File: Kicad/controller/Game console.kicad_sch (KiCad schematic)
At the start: 6 parts, among them SW1 SW_Push, SW2 SW_Push, SW3 SW_Push

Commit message: writing firmware codee
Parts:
- removed RV1, RV2: R_Potentiometer, symbol Device:R_Potentiometer
- removed SW1, SW2: SW_Push, symbol Switch:SW_Push
- added C1, C2: 100nF, Capacitor_THT:C_Disc_D5.0mm_W2.5mm_P2.50mm, symbol Device:C
- added Left1, Right1: RKJXV1224005, easyeda2kicad:SW-TH_RKJXV1224005, symbol easyeda2kicad:RKJXV1224005
- added SW1: LB, easyeda2kicad:SW-TH_TC-1102N-C-DL-B, symbol easyeda2kicad:TC-1102N-C-DL-B
- added SW10: B, Button_Switch_THT:SW_PUSH_6mm_H5mm, symbol Switch:SW_Push
- added SW11: Menu, Button_Switch_THT:SW_PUSH_6mm_H5mm, symbol Switch:SW_Push
- added SW12: X, Button_Switch_THT:SW_PUSH_6mm_H5mm, symbol Switch:SW_Push
- added SW13: Y, Button_Switch_THT:SW_PUSH_6mm_H5mm, symbol Switch:SW_Push
- added SW14: View, Button_Switch_THT:SW_PUSH_6mm_H5mm, symbol Switch:SW_Push
- added SW15: LT, easyeda2kicad:SW-TH_TC-1102N-C-DL-B, symbol easyeda2kicad:TC-1102N-C-DL-B
- added SW16: RT, easyeda2kicad:SW-TH_TC-1102N-C-DL-B, symbol easyeda2kicad:TC-1102N-C-DL-B
- added SW2: RB, easyeda2kicad:SW-TH_TC-1102N-C-DL-B, symbol easyeda2kicad:TC-1102N-C-DL-B
- added SW4: D Pad right, Button_Switch_THT:SW_PUSH_6mm_H5mm, symbol Switch:SW_Push
- added SW5: D Pad Left, Button_Switch_THT:SW_PUSH_6mm_H5mm, symbol Switch:SW_Push
- added SW6: A, Button_Switch_THT:SW_PUSH_6mm_H5mm, symbol Switch:SW_Push
- added SW7: D Pad bottom, Button_Switch_THT:SW_PUSH_6mm_H5mm, symbol Switch:SW_Push
- added SW8: Reset, Button_Switch_THT:SW_PUSH_6mm_H5mm, symbol Switch:SW_Push
- added SW9: Home, Button_Switch_THT:SW_PUSH_6mm_H5mm, symbol Switch:SW_Push
- added U1: MCP3008, Package_DIP:DIP-16_W7.62mm, symbol Analog_ADC:MCP3008
- SW3: value SW_Push -> D Pad top; footprint (none) -> Button_Switch_THT:SW_PUSH_6mm_H5mm
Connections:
- net at SW3.1: now also A1.19 (GPIO14)
- net at SW3.2: now also A1.13 (GND), A1.18 (GND), A1.23 (GND), A1.28 (GND), A1.3 (GND), A1.33 (AGND), A1.38 (GND), A1.8 (GND), C1.2, C2.2, Left1.1 (B), Left1.10 (GND), Left1.6 (B), Left1.7 (GND), Left1.8 (GND), Left1.9 (GND), Left1.b, Right1.1 (B), Right1.10 (GND), Right1.6 (B), Right1.7 (GND), Right1.8 (GND), Right1.9 (GND), Right1.b, SW1.2, SW1.3, SW1.4, SW10.2, SW11.2, SW12.2, SW13.2, SW14.2, SW15.2, SW15.3, SW15.4, SW16.2, SW16.3, SW16.4, SW2.2, SW2.3, SW2.4, SW4.2, SW5.2, SW6.2, SW7.2, SW8.2, SW9.2, U1.14 (AGND), U1.9 (DGND)
- net at A1.36 (3V3): now also C1.1, C2.1, Left1.3 (A), Left1.4 (A), Right1.3 (A), Right1.4 (A), U1.15 (Vref), U1.16 (Vdd)
- net at A1.1 (GPIO0): now also SW14.1
- net at A1.10 (GPIO7): now also SW13.1
- net at A1.11 (GPIO8): now also SW12.1
- net at A1.12 (GPIO9): now also SW10.1
- net at A1.14 (GPIO10): now also SW6.1
- net at A1.15 (GPIO11): now also SW4.1
- net at A1.16 (GPIO12): now also SW5.1
- net at A1.17 (GPIO13): now also SW7.1
- net at A1.2 (GPIO1): now also SW9.1
- net at A1.21 (GPIO16): now also U1.12 (Dout)
- net at A1.22 (GPIO17): now also U1.10 (~{CS}/SHDN)
- net at A1.24 (GPIO18): now also U1.13 (CLK)
- net at A1.25 (GPIO19): now also U1.11 (Din)
- net at A1.30 (RUN): now also SW8.1
- net at A1.31 (GPIO26_ADC0): now also Left1.a
- net at A1.32 (GPIO27_ADC1): now also Right1.a
- net at A1.4 (GPIO2): now also SW11.1
- net at A1.5 (GPIO3): now also SW16.1
- net at A1.6 (GPIO4): now also SW2.1
- net at A1.7 (GPIO5): now also SW15.1
- net at A1.9 (GPIO6): now also SW1.1
- new net: Left1.2 (DTA), U1.1 (CH0)
- new net: Left1.5 (DTA), U1.2 (CH1)
- new net: Right1.2 (DTA), U1.3 (CH2)
- new net: Right1.5 (DTA), U1.4 (CH3)
- no-connect marks 0 -> 17

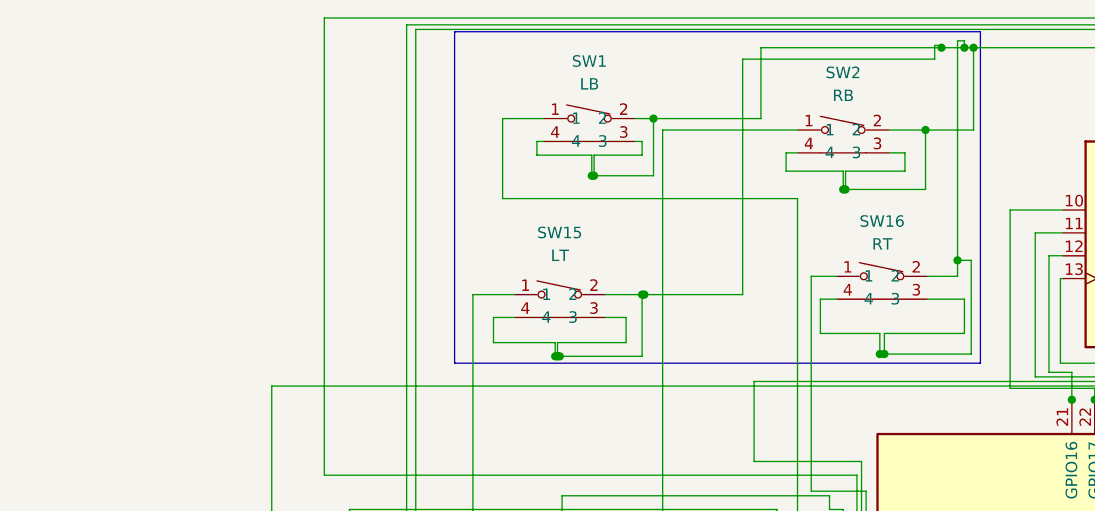
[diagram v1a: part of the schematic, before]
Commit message: basic cad complete and new shoulder board created for rb, lb, rt and lt triggers
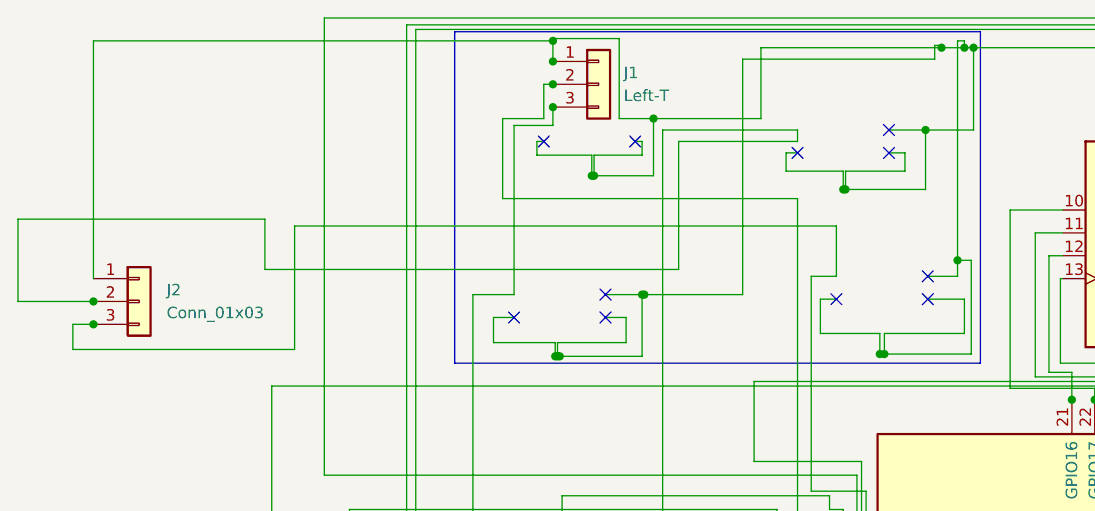
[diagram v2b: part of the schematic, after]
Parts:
- removed SW1: LB, easyeda2kicad:SW-TH_TC-1102N-C-DL-B, symbol easyeda2kicad:TC-1102N-C-DL-B
- removed SW15: LT, easyeda2kicad:SW-TH_TC-1102N-C-DL-B, symbol easyeda2kicad:TC-1102N-C-DL-B
- removed SW16: RT, easyeda2kicad:SW-TH_TC-1102N-C-DL-B, symbol easyeda2kicad:TC-1102N-C-DL-B
- removed SW2: RB, easyeda2kicad:SW-TH_TC-1102N-C-DL-B, symbol easyeda2kicad:TC-1102N-C-DL-B
- added J1: Left-T, Connector_JST:JST_XH_B3B-XH-A_1x03_P2.50mm_Vertical, symbol Connector_Generic:Conn_01x03
- added J2: Conn_01x03, Connector_JST:JST_XH_B3B-XH-A_1x03_P2.50mm_Vertical, symbol Connector_Generic:Conn_01x03
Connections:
- net at A1.13 (GND), A1.18 (GND), A1.23 (GND)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: now also J1.1 (Pin_1), J2.1 (Pin_1)
- net at A1.6 (GPIO4): now also J2.2 (Pin_2)
- net at A1.9 (GPIO6): now also J1.2 (Pin_2)
- net at A1.5 (GPIO3): now also J2.3 (Pin_3)
- net at A1.7 (GPIO5): now also J1.3 (Pin_3)
- no-connect marks 17 -> 28

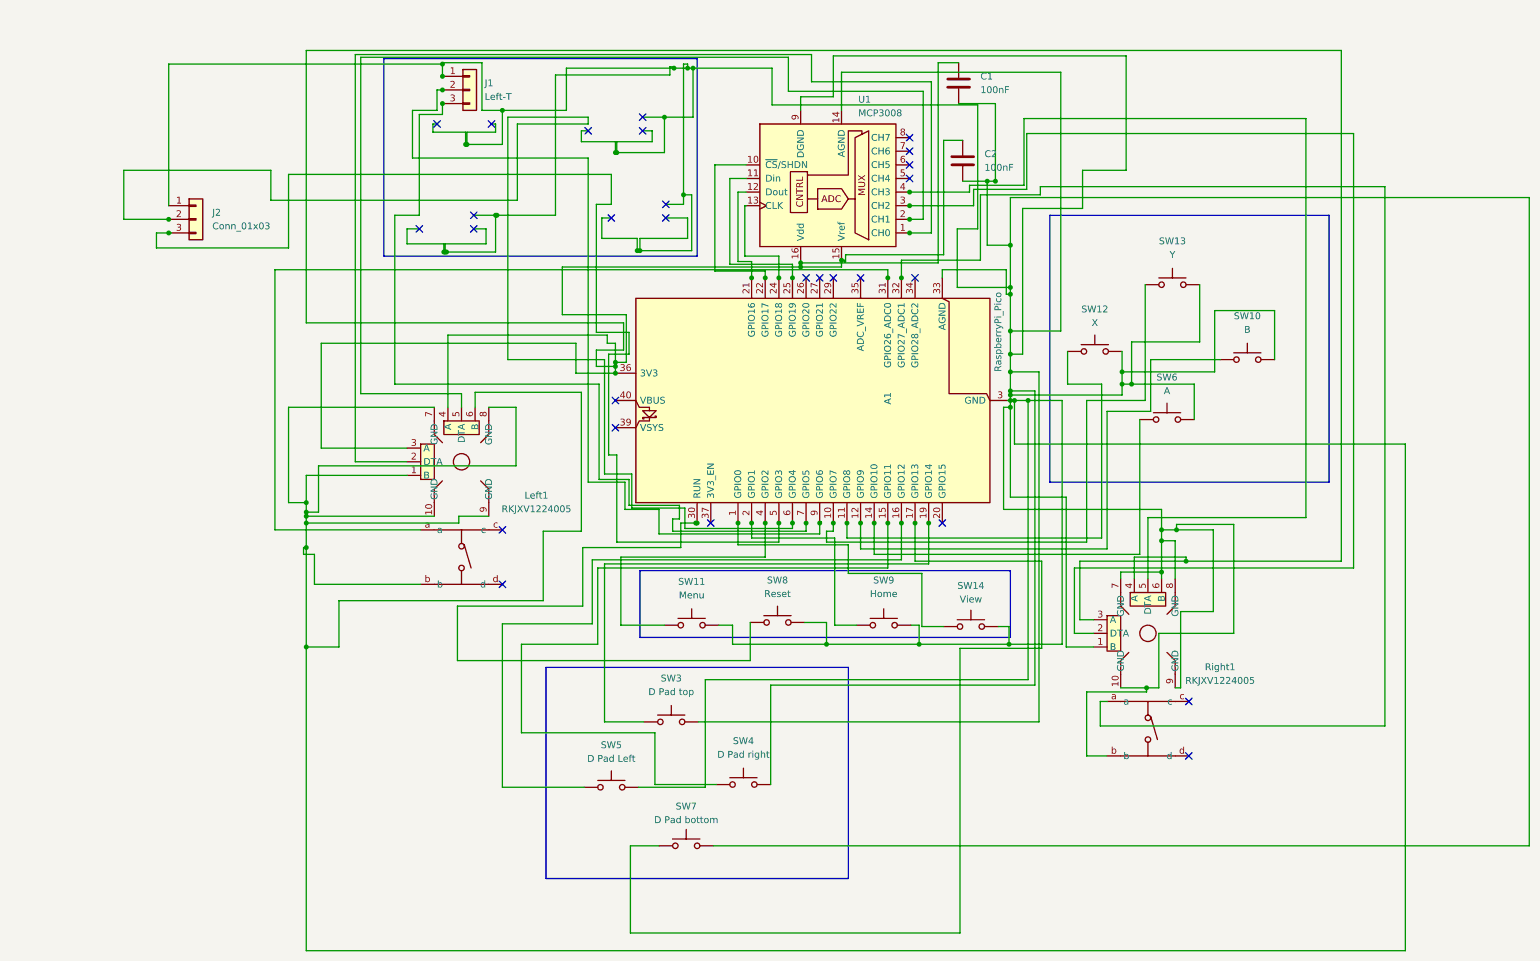
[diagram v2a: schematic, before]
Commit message: changes in schematic to add vibration motors for controller and led
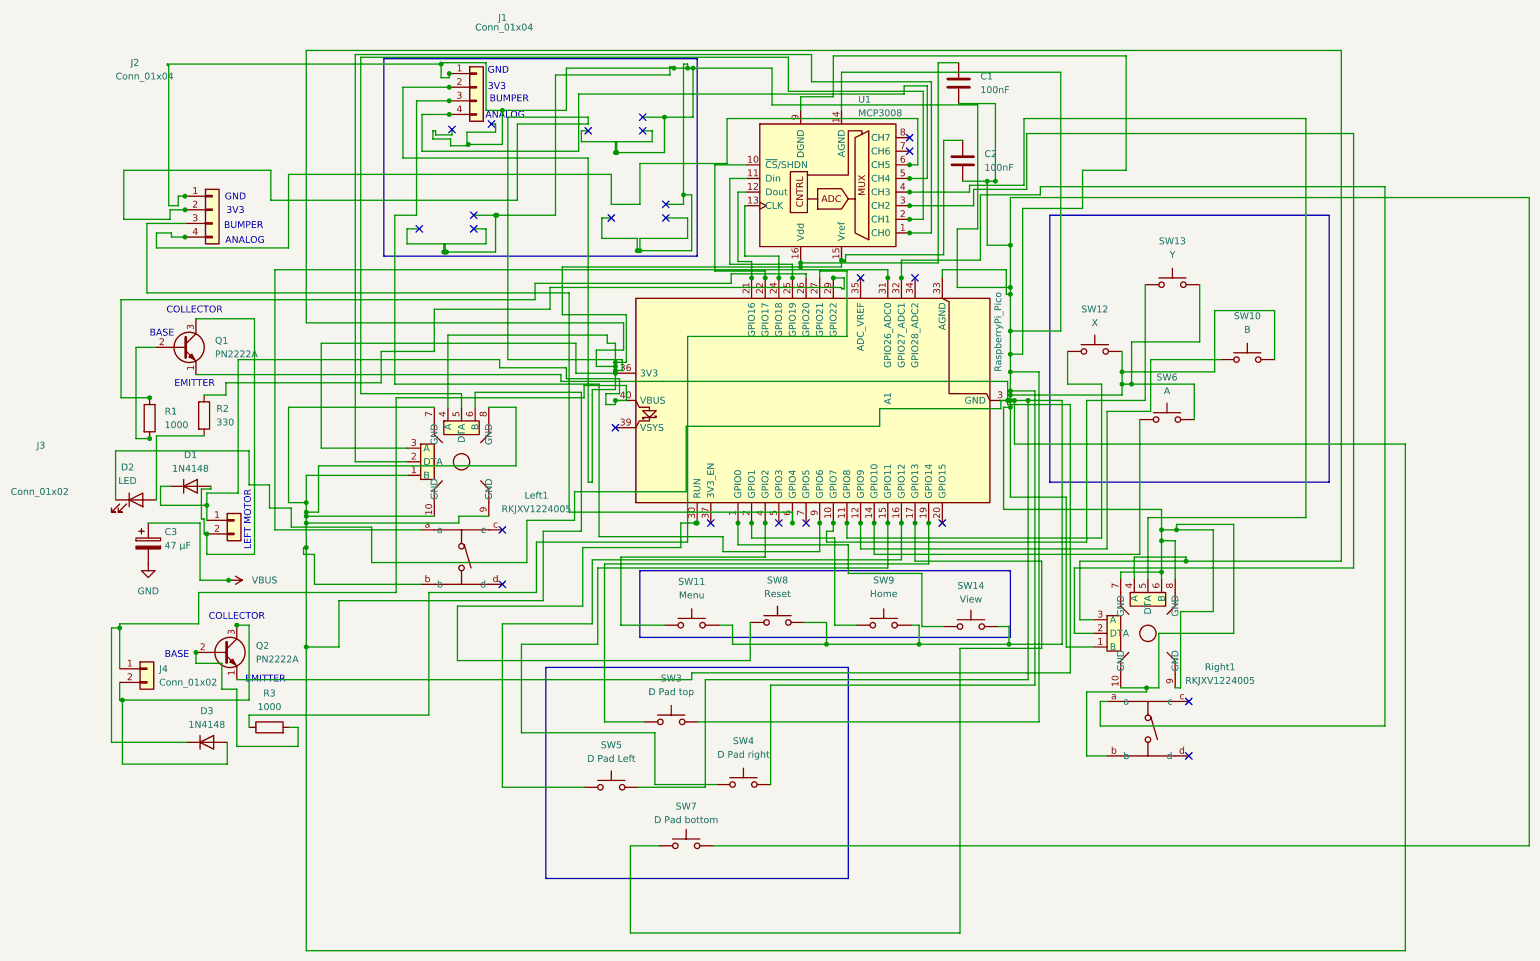
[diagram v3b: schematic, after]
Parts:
- removed J1: Left-T, Connector_JST:JST_XH_B3B-XH-A_1x03_P2.50mm_Vertical, symbol Connector_Generic:Conn_01x03
- removed J2: Conn_01x03, Connector_JST:JST_XH_B3B-XH-A_1x03_P2.50mm_Vertical, symbol Connector_Generic:Conn_01x03
- added C3: 47 µF, symbol Device:C_Polarized
- added D1, D3: 1N4148, Diode_THT:D_DO-35_SOD27_P7.62mm_Horizontal, symbol Diode:1N4148
- added D2: LED, symbol Device:LED
- added J1, J2: Conn_01x04, Connector_JST:JST_XH_B4B-XH-A_1x04_P2.50mm_Vertical, symbol Connector_Generic:Conn_01x04
- added J3, J4: Conn_01x02, symbol Connector_Generic:Conn_01x02
- added Q1, Q2: PN2222A, Package_TO_SOT_THT:TO-92_Inline, symbol Transistor_BJT:PN2222A
- added R1, R3: 1000, symbol Device:R
- added R2: 330, symbol Device:R
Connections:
- net at A1.13 (GND), A1.18 (GND), A1.23 (GND)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: now also J1.1 (Pin_1), J2.1 (Pin_1), Q1.1 (E), Q2.1 (E)
- net at A1.36 (3V3), C1.1, C2.1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: now also J1.2 (Pin_2), J2.2 (Pin_2)
- net at A1.6 (GPIO4): now also J2.3 (Pin_3)
- net at U1.5 (CH4): now also J1.4 (Pin_4)
- net at U1.6 (CH5): now also J2.4 (Pin_4)
- net at A1.9 (GPIO6): now also J1.3 (Pin_3)
- net at A1.26 (GPIO20): now also R1.1
- net at A1.27 (GPIO21): now also R3.1
- net at A1.29 (GPIO22): now also R2.1
- net at A1.40 (VBUS): now also D1.1 (K), D3.1 (K), J3.1 (Pin_1), J4.1 (Pin_1)
- new net: Q1.2 (B), R1.2
- new net: D1.2 (A), J3.2 (Pin_2), Q1.3 (C)
- new net: D3.2 (A), J4.2 (Pin_2), Q2.3 (C)
- new net: D2.2 (A), R2.2
- new net: Q2.2 (B), R3.2
- new net GND: C3.2
- new net VBUS: C3.1
- no-connect marks 28 -> 24
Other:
- note added: "3V3"
- note added: "ANALOG"
- note added: "BASE"
- note added: "BUMPER"
- note added: "COLLECTOR"
- note added: "EMITTER"
- note added: "GND"
- note added: "LEFT MOTOR"

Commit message: doing the layout for pcb so I can make the perfect pcb board
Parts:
- C3: footprint (none) -> Capacitor_THT:CP_Radial_D5.0mm_P2.00mm
- D2: footprint (none) -> LED_THT:LED_D3.0mm
- J3, J4: footprint (none) -> Connector_JST:JST_PH_B2B-PH-K_1x02_P2.00mm_Vertical
- R1, R2, R3: footprint (none) -> Resistor_THT:R_Axial_DIN0207_L6.3mm_D2.5mm_P10.16mm_Horizontal
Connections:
- net GND: now also D2.1 (K)
- net VBUS: now also A1.40 (VBUS), D1.1 (K), D3.1 (K), J3.1 (Pin_1), J4.1 (Pin_1)
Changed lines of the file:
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@@
 	)
 	(junction
+		(at 179.07 77.47)
+		(diameter 0)
+		(color 0 0 0 0)
+	)
+	(junction
 		(at 201.422 72.136)
 		(diameter 0)
@@
 	(wire
 		(pts
-			(xy 156.21 78.994) (xy 178.816 78.994)
-		)
-		(stroke
-			(width 0)
-			(type default)
-		)
-	)
-	(wire
-		(pts
 			(xy 149.86 51.562) (xy 149.606 51.562)
 		)
@@
 	(wire
 		(pts
+			(xy 179.07 77.47) (xy 179.832 77.47)
+		)
+		(stroke
+			(width 0)
+			(type default)
+		)
+	)
+	(wire
+		(pts
 			(xy 155.194 100.076) (xy 155.194 100.33)
 		)
@@
 	(wire
 		(pts
-			(xy 178.816 78.994) (xy 178.816 77.47)
-		)
-		(stroke
-			(width 0)
-			(type default)
-		)
-	)
-	(wire
-		(pts
 			(xy 215.9 66.548) (xy 203.2 66.548)
 		)
@@
 	(wire
 		(pts
-			(xy 178.816 77.47) (xy 179.832 77.47)
-		)
-		(stroke
-			(width 0)
-			(type default)
-		)
-	)
-	(wire
-		(pts
 			(xy 88.392 89.662) (xy 51.562 89.662)
 		)
@@
 	(wire
 		(pts
+			(xy 178.816 77.47) (xy 179.07 77.47)
+		)
+		(stroke
+			(width 0)
+			(type default)
+		)
+	)
+	(wire
+		(pts
 			(xy 93.472 101.854) (xy 93.472 114.808)
 		)
@@
 	(wire
 		(pts
+			(xy 177.8 77.978) (xy 179.07 77.978)
+		)
+		(stroke
+			(width 0)
+			(type default)
+		)
+	)
+	(wire
+		(pts
 			(xy 162.814 100.33) (xy 162.814 107.442)
 		)
@@
 	(wire
 		(pts
+			(xy 179.07 77.978) (xy 179.07 77.47)
+		)
+		(stroke
+			(width 0)
+			(type default)
+		)
+	)
+	(wire
+		(pts
 			(xy 128.27 36.068) (xy 128.27 52.07)
 		)
@@
 	(wire
 		(pts
+			(xy 156.21 78.994) (xy 177.8 78.994)
+		)
+		(stroke
+			(width 0)
+			(type default)
+		)
+	)
+	(wire
+		(pts
+			(xy 177.8 78.994) (xy 177.8 77.978)
+		)
+		(stroke
+			(width 0)
+			(type default)
+		)
+	)
+	(wire
+		(pts
 			(xy 129.794 100.33) (xy 129.794 104.394)
 		)
@@
 			)
 		)
-		(property "Footprint" ""
+		(property "Footprint" "Connector_JST:JST_PH_B2B-PH-K_1x02_P2.00mm_Vertical"
 			(at 35.814 99.822 0)
 			(hide yes)
@@
 	)
 	(symbol
+		(lib_id "power:GND")
+		(at 179.07 77.47 0)
+		(unit 1)
+		(body_style 1)
+		(exclude_from_sim no)
+		(in_bom yes)
+		(on_board yes)
+		(in_pos_files yes)
+		(dnp no)
+		(fields_autoplaced yes)
+		(property "Reference" "#PWR04"
+			(at 179.07 83.82 0)
+			(hide yes)
+			(show_name no)
+			(do_not_autoplace no)
+			(effects
+				(font
+					(size 1.27 1.27)
+				)
+			)
+		)
+		(property "Value" "GND"
+			(at 179.07 82.55 0)
+			(show_name no)
+			(do_not_autoplace no)
+			(effects
+				(font
+					(size 1.27 1.27)
+				)
+			)
+		)
+		(property "Footprint" ""
+			(at 179.07 77.47 0)
+			(hide yes)
+			(show_name no)
+			(do_not_autoplace no)
+			(effects
+				(font
+					(size 1.27 1.27)
+				)
+			)
+		)
+		(property "Datasheet" ""
+			(at 179.07 77.47 0)
+			(hide yes)
+			(show_name no)
+			(do_not_autoplace no)
+			(effects
+				(font
+					(size 1.27 1.27)
+				)
+			)
+		)
+		(property "Description" "Power symbol creates a global label with name \"GND\" , ground"
+			(at 179.07 77.47 0)
+			(hide yes)
+			(show_name no)
+			(do_not_autoplace no)
+			(effects
+				(font
+					(size 1.27 1.27)
+				)
+			)
+		)
+		(pin "1"
+		)
+		(instances
+			(project "Game console"
+				(path "/5d92d208-f11d-47b0-aded-0294da1c15f0"
+					(reference "#PWR04")
+					(unit 1)
+				)
+			)
+		)
+	)
+	(symbol
 		(lib_id "Switch:SW_Push")
 		(at 156.972 119.38 0)
@@
 			)
 		)
-		(property "Footprint" ""
+		(property "Footprint" "Capacitor_THT:CP_Radial_D5.0mm_P2.00mm"
 			(at 20.7772 107.95 0)
 			(hide yes)
@@
 			)
 		)
-		(property "Footprint" ""
+		(property "Footprint" "LED_THT:LED_D3.0mm"
 			(at 17.526 96.012 0)
 			(hide yes)
@@
 			)
 		)
-		(property "Footprint" ""
+		(property "Footprint" "Resistor_THT:R_Axial_DIN0207_L6.3mm_D2.5mm_P10.16mm_Horizontal"
 			(at 42.418 140.208 90)
 			(hide yes)
@@
 			)
 		)
-		(property "Footprint" ""
+		(property "Footprint" "Resistor_THT:R_Axial_DIN0207_L6.3mm_D2.5mm_P10.16mm_Horizontal"
 			(at 18.288 80.772 90)
 			(hide yes)
@@
 			)
 		)
-		(property "Footprint" ""
+		(property "Footprint" "Resistor_THT:R_Axial_DIN0207_L6.3mm_D2.5mm_P10.16mm_Horizontal"
 			(at 28.448 80.264 90)
 			(hide yes)
@@
 			)
 		)
-		(property "Footprint" ""
+		(property "Footprint" "Connector_JST:JST_PH_B2B-PH-K_1x02_P2.00mm_Vertical"
 			(at 19.558 127.508 0)
 			(hide yes)
@@
 					(unit 1)
 				)
+			)
+		)
+	)
+	(symbol
+		(lib_id "power:VBUS")
+		(at 106.934 77.47 180)
+		(unit 1)
+		(body_style 1)
+		(exclude_from_sim no)
+		(in_bom yes)
+		(on_board yes)
+		(in_pos_files yes)
+		(dnp no)
+		(fields_autoplaced yes)
+		(property "Reference" "#PWR03"
+			(at 106.934 73.66 0)
+			(hide yes)
+			(show_name no)
+			(do_not_autoplace no)
+			(effects
+				(font
+					(size 1.27 1.27)
+				)
+			)
+		)
+		(property "Value" "VBUS"
+			(at 106.934 82.55 0)
+			(show_name no)
+			(do_not_autoplace no)
+			(effects
+				(font
+					(size 1.27 1.27)
+				)
+			)
+		)
+		(property "Footprint" ""
+			(at 106.934 77.47 0)
+			(hide yes)
+			(show_name no)
+			(do_not_autoplace no)
+			(effects
+				(font
+					(size 1.27 1.27)
+				)
+			)
+		)
+		(property "Datasheet" ""
+			(at 106.934 77.47 0)
+			(hide yes)
+			(show_name no)
+			(do_not_autoplace no)
+			(effects
+				(font
+					(size 1.27 1.27)
+				)
+			)
+		)
+		(property "Description" "Power symbol creates a global label with name \"VBUS\""
+			(at 106.934 77.47 0)
+			(hide yes)
+			(show_name no)
+			(do_not_autoplace no)
+			(effects
+				(font
+					(size 1.27 1.27)
+				)
+			)
+		)
+		(pin "1"
+		)
+		(instances
+			(project "Game console"
+				(path "/5d92d208-f11d-47b0-aded-0294da1c15f0"
+					(reference "#PWR03")
+					(unit 1)
+				)
